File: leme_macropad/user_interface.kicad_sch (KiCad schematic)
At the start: 23 parts, among them J2 OLED display, SW1 RotaryEncoder_Switch, SW10 SW_Push, SW2 SW_Push, SW3 SW_Push, SW4 SW_Push, SW5 SW_Push, SW6 SW_Push, SW7 SW_Push, SW8 SW_Push, SW9 SW_Push

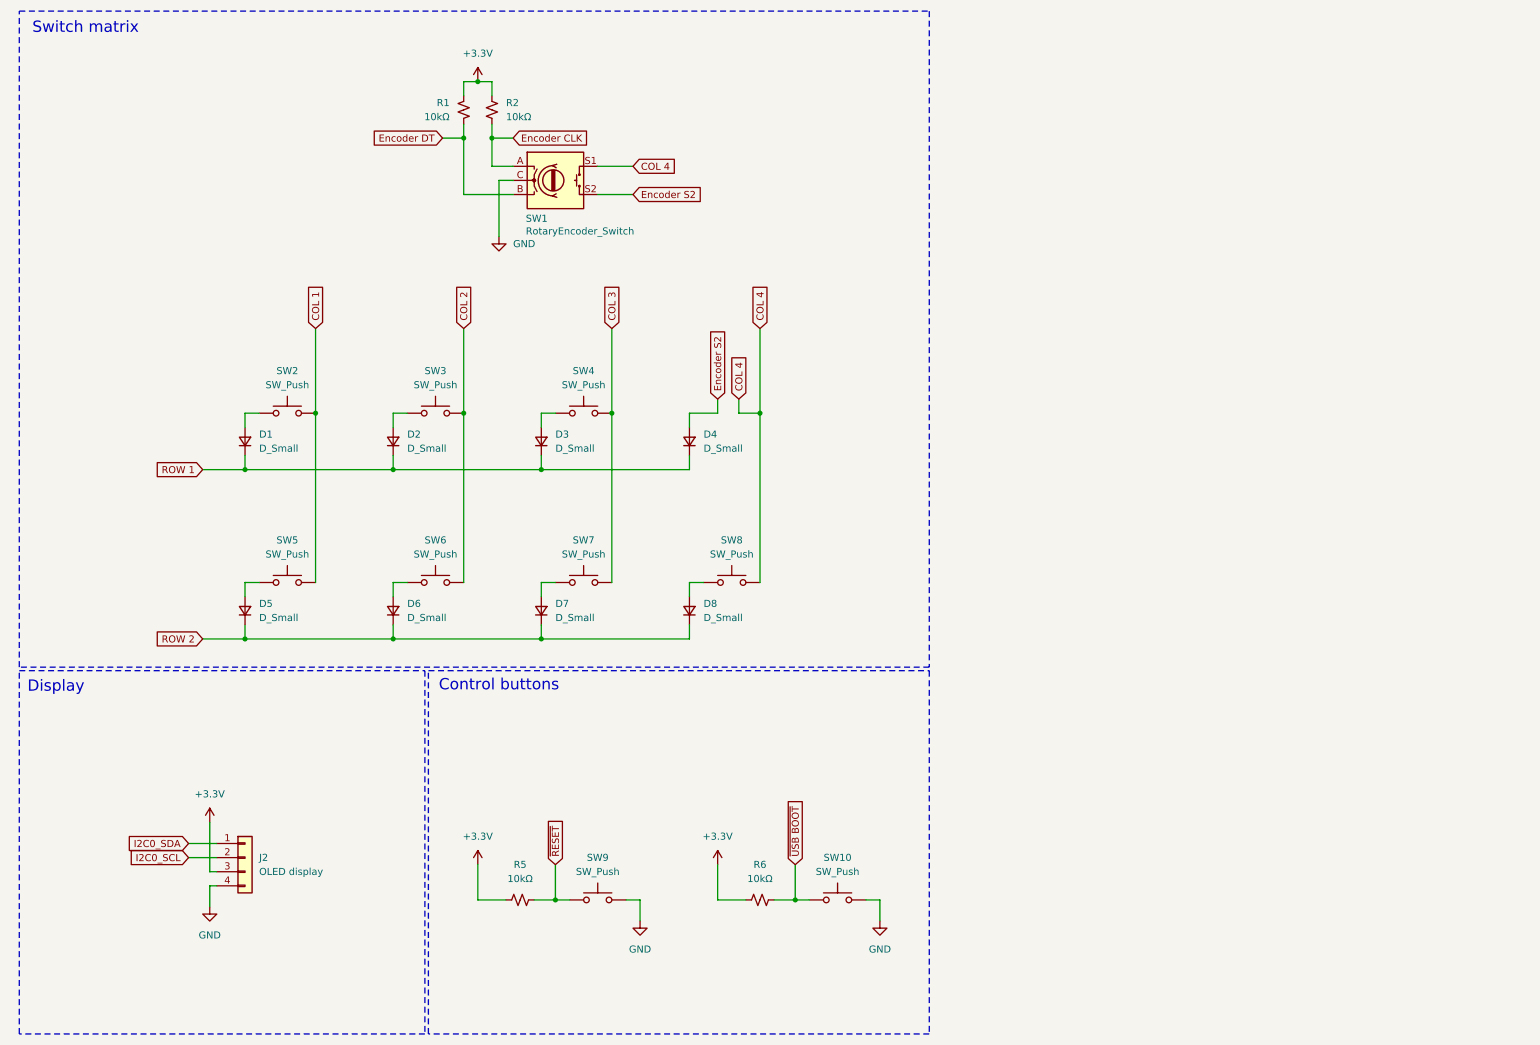
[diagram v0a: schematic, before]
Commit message: Adds RGB LED matrix
There's only one per switch for now.
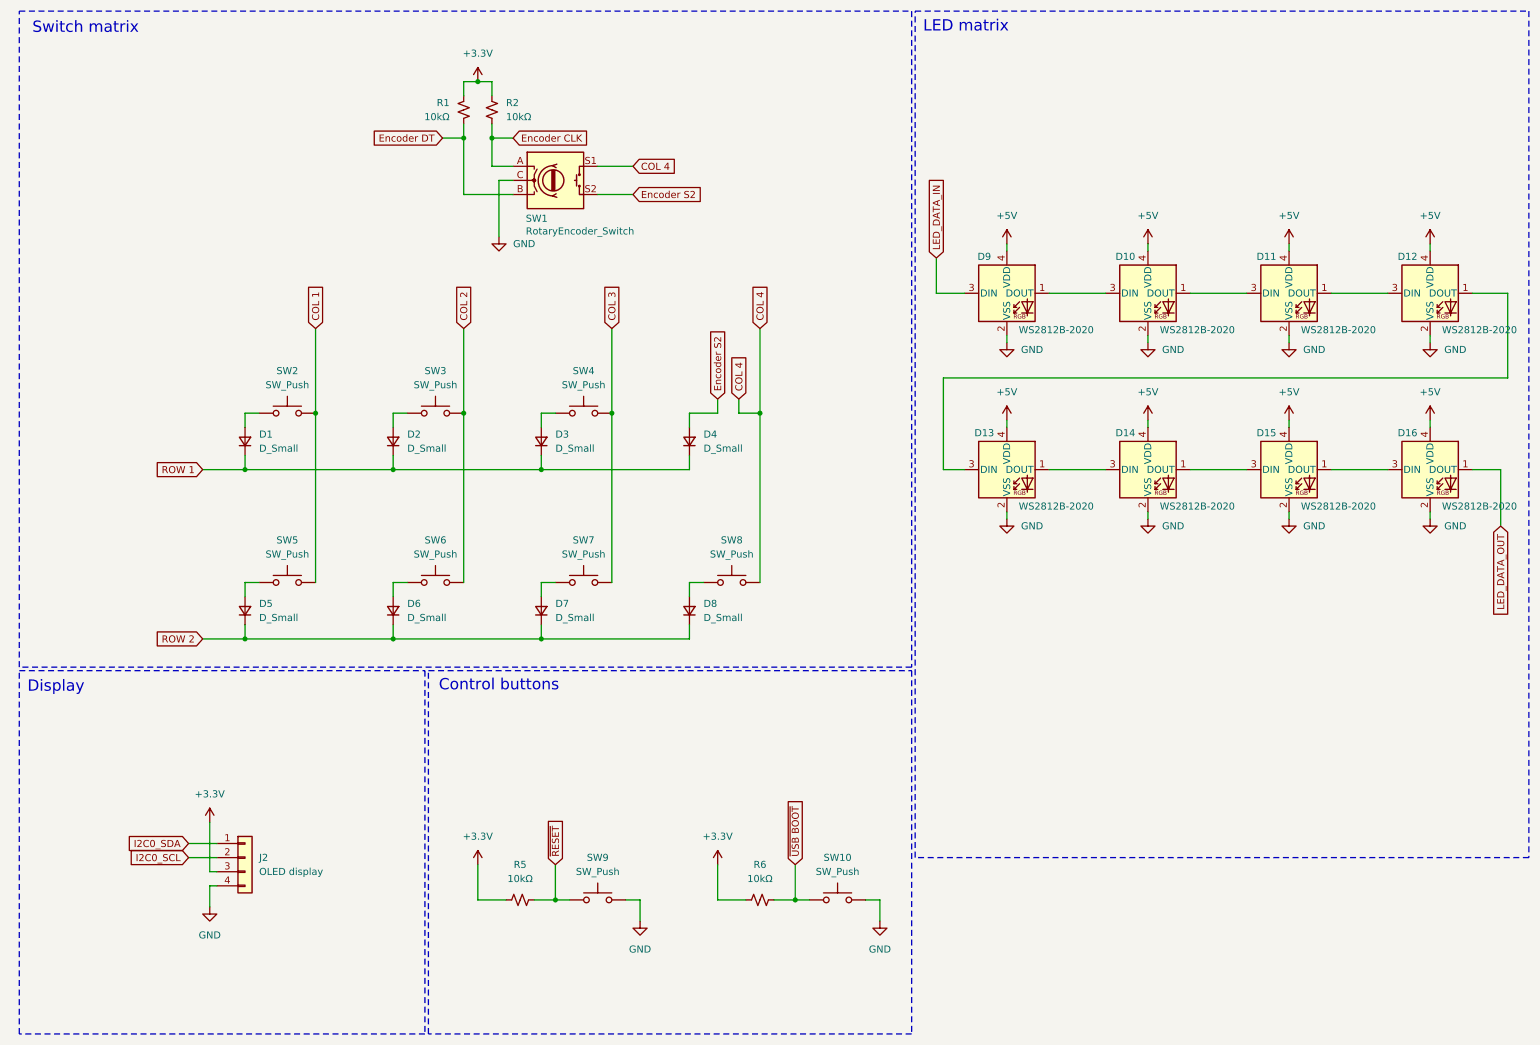
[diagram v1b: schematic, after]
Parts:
- added D10, D11, D12, D13, D14, D15, D16, D9: WS2812B-2020, LED_SMD:LED_WS2812B-2020_PLCC4_2.0x2.0mm, symbol LED:WS2812B-2020
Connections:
- net GND: now also D10.2 (VSS), D11.2 (VSS), D12.2 (VSS), D13.2 (VSS), D14.2 (VSS), D15.2 (VSS), D16.2 (VSS), D9.2 (VSS)
- new net: D14.1 (DOUT), D15.3 (DIN)
- new net: D13.1 (DOUT), D14.3 (DIN)
- new net: D10.3 (DIN), D9.1 (DOUT)
- new net: D12.1 (DOUT), D13.3 (DIN)
- new net: D11.1 (DOUT), D12.3 (DIN)
- new net: D15.1 (DOUT), D16.3 (DIN)
- new net: D10.1 (DOUT), D11.3 (DIN)
- new net +5V: D10.4 (VDD), D11.4 (VDD), D12.4 (VDD), D13.4 (VDD), D14.4 (VDD), D15.4 (VDD), D16.4 (VDD), D9.4 (VDD)
- new net LED_DATA_IN: D9.3 (DIN)
- new net LED_DATA_OUT: D16.1 (DOUT)
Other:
- note added: "LED matrix"

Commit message: Re-annotates schematics
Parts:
- renumbered D5 to D2, D2 to D3, D6 to D4, D3 to D5, D7 to D6, D4 to D7, R2 to R10, R6 to R11, R5 to R8, R1 to R9, SW2 to SW1, SW5 to SW2, SW6 to SW4, SW4 to SW5, SW7 to SW6, SW1 to SW7
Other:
- moved on the sheet: D1, D2, D3, D4, D5, D6, D7, D8, R10, R9, SW1, SW2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

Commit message: Assigns footprints to all components in schematics
Passives are 0603, but if the layout gets too dificult (specially around
the RP2040) we might want to decrease the size.

The mechanical switches are set as hotswap sockets for Kailh v1/v2, but
after routing everything we might want to do a version for MX switches.
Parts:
- D1, D2, D3, D4, D5, D6, D7, D8: footprint (none) -> Diode_SMD:D_SOD-123
- J2: footprint (none) -> Connector_PinHeader_2.54mm:PinHeader_1x04_P2.54mm_Vertical
- R10, R11, R8, R9: footprint (none) -> Resistor_SMD:R_0603_1608Metric_Pad0.98x0.95mm_HandSolder
- SW1, SW2, SW3, SW4, SW5, SW6: footprint (none) -> PCM_Switch_Keyboard_Hotswap_Kailh:SW_Hotswap_Kailh_Choc_V1V2_1.00u
- SW10, SW8, SW9: footprint (none) -> leme_macropad:CK_PTS636_SK43_SMTR_LFS
- SW7: footprint (none) -> Rotary_Encoder:RotaryEncoder_Alps_EC11E-Switch_Vertical_H20mm
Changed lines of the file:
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@@
 			)
 		)
-		(property "Footprint" ""
+		(property "Footprint" "leme_macropad:CK_PTS636_SK43_SMTR_LFS"
 			(at 160.02 167.64 0)
 			(effects
@@
 			)
 		)
-		(property "Footprint" ""
+		(property "Footprint" "Diode_SMD:D_SOD-123"
 			(at 87.63 90.17 90)
 			(effects
@@
 			)
 		)
-		(property "Footprint" ""
+		(property "Footprint" "Diode_SMD:D_SOD-123"
 			(at 60.96 90.17 90)
 			(effects
@@
 			)
 		)
-		(property "Footprint" ""
+		(property "Footprint" "Diode_SMD:D_SOD-123"
 			(at 34.29 120.65 90)
 			(effects
@@
 			)
 		)
-		(property "Footprint" ""
+		(property "Footprint" "Resistor_SMD:R_0603_1608Metric_Pad0.98x0.95mm_HandSolder"
 			(at 113.03 30.48 0)
 			(effects
@@
 			)
 		)
-		(property "Footprint" ""
+		(property "Footprint" "Resistor_SMD:R_0603_1608Metric_Pad0.98x0.95mm_HandSolder"
 			(at 146.05 172.72 0)
 			(effects
@@
 			)
 		)
-		(property "Footprint" ""
+		(property "Footprint" "Rotary_Encoder:RotaryEncoder_Alps_EC11E-Switch_Vertical_H20mm"
 			(at 120.65 39.116 0)
 			(effects
@@
 			)
 		)
-		(property "Footprint" ""
+		(property "Footprint" "Diode_SMD:D_SOD-123"
 			(at 114.3 90.17 90)
 			(effects
@@
 			)
 		)
-		(property "Footprint" ""
+		(property "Footprint" "PCM_Switch_Keyboard_Hotswap_Kailh:SW_Hotswap_Kailh_Choc_V1V2_1.00u"
 			(at 41.91 110.49 0)
 			(effects
@@
 			)
 		)
-		(property "Footprint" ""
+		(property "Footprint" "Diode_SMD:D_SOD-123"
 			(at 114.3 120.65 90)
 			(effects
@@
 			)
 		)
-		(property "Footprint" ""
+		(property "Footprint" "leme_macropad:CK_PTS636_SK43_SMTR_LFS"
 			(at 116.84 167.64 0)
 			(effects
@@
 			)
 		)
-		(property "Footprint" ""
+		(property "Footprint" "PCM_Switch_Keyboard_Hotswap_Kailh:SW_Hotswap_Kailh_Choc_V1V2_1.00u"
 			(at 68.58 110.49 0)
 			(effects
@@
 			)
 		)
-		(property "Footprint" ""
+		(property "Footprint" "PCM_Switch_Keyboard_Hotswap_Kailh:SW_Hotswap_Kailh_Choc_V1V2_1.00u"
 			(at 95.25 80.01 0)
 			(effects
@@
 			)
 		)
-		(property "Footprint" ""
+		(property "Footprint" "Connector_PinHeader_2.54mm:PinHeader_1x04_P2.54mm_Vertical"
 			(at 53.34 165.1 0)
 			(effects
@@
 			)
 		)
-		(property "Footprint" ""
+		(property "Footprint" "PCM_Switch_Keyboard_Hotswap_Kailh:SW_Hotswap_Kailh_Choc_V1V2_1.00u"
 			(at 41.91 80.01 0)
 			(effects
@@
 			)
 		)
-		(property "Footprint" ""
+		(property "Footprint" "Diode_SMD:D_SOD-123"
 			(at 34.29 90.17 90)
 			(effects
@@
 			)
 		)
-		(property "Footprint" ""
+		(property "Footprint" "Diode_SMD:D_SOD-123"
 			(at 87.63 120.65 90)
 			(effects
@@
 			)
 		)
-		(property "Footprint" ""
+		(property "Footprint" "Resistor_SMD:R_0603_1608Metric_Pad0.98x0.95mm_HandSolder"
 			(at 107.95 30.48 0)
 			(effects
@@
 			)
 		)
-		(property "Footprint" ""
+		(property "Footprint" "PCM_Switch_Keyboard_Hotswap_Kailh:SW_Hotswap_Kailh_Choc_V1V2_1.00u"
 			(at 95.25 110.49 0)
 			(effects
@@
 			)
 		)
-		(property "Footprint" ""
+		(property "Footprint" "Diode_SMD:D_SOD-123"
 			(at 60.96 120.65 90)
 			(effects
@@
 			)
 		)
-		(property "Footprint" ""
+		(property "Footprint" "PCM_Switch_Keyboard_Hotswap_Kailh:SW_Hotswap_Kailh_Choc_V1V2_1.00u"
 			(at 68.58 80.01 0)
 			(effects
@@
 			)
 		)
-		(property "Footprint" ""
+		(property "Footprint" "Resistor_SMD:R_0603_1608Metric_Pad0.98x0.95mm_HandSolder"
 			(at 102.87 172.72 0)
 			(effects
@@
 			)
 		)
-		(property "Footprint" ""
+		(property "Footprint" "leme_macropad:CK_PTS636_SK43_SMTR_LFS"
 			(at 121.92 110.49 0)
 			(effects

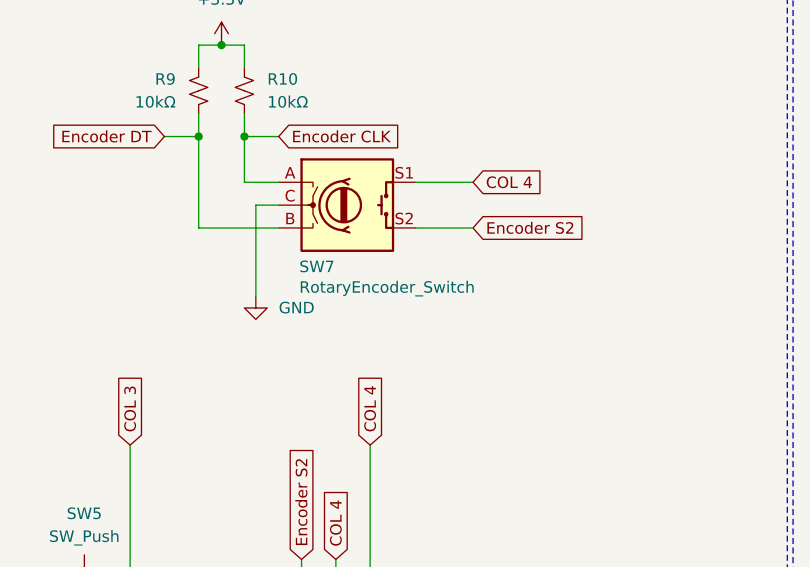
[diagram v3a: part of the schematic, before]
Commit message: Uses rotary encoder symbol with mounting pin
The rotary switch we'll use has mounting pins that can be soldered.
Since they're connected to the chassis, they're now connected to ground
in the schematics.

This change fixes a warning when importing the schematics to the PCB
editor.
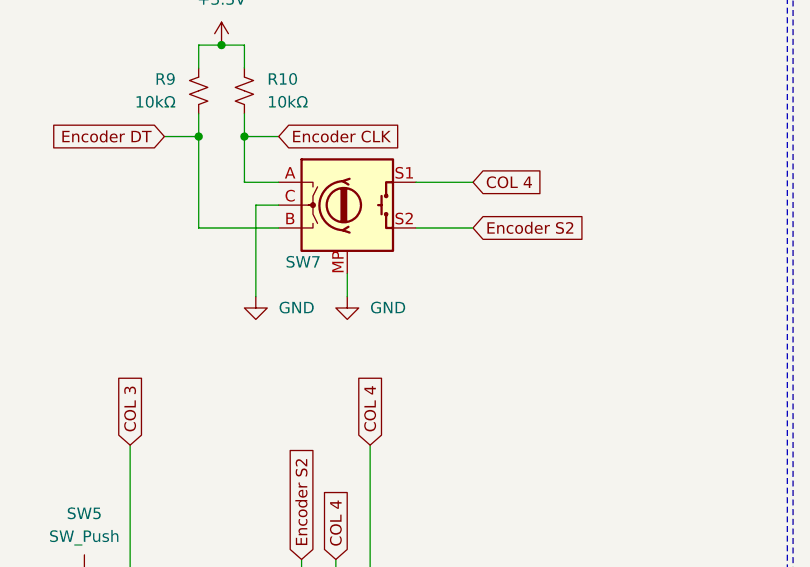
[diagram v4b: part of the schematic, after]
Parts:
- SW7: symbol Device:RotaryEncoder_Switch -> Device:RotaryEncoder_Switch_MP
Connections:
- net GND: now also SW7.MP
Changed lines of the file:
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@@
+	(wire
+		(pts
+			(xy 124.46 50.8) (xy 124.46 53.34)
+		)
+		(stroke
+			(width 0)
+			(type default)
+		)
+	)
 	(wire
 		(pts
@@
 	)
 	(symbol
+		(lib_id "power:GND")
+		(at 124.46 53.34 0)
+		(unit 1)
+		(exclude_from_sim no)
+		(in_bom yes)
+		(on_board yes)
+		(dnp no)
+		(fields_autoplaced yes)
+		(property "Reference" "#PWR063"
+			(at 124.46 59.69 0)
+			(effects
+				(font
+					(size 1.27 1.27)
+				)
+				(hide yes)
+			)
+		)
+		(property "Value" "GND"
+			(at 127 54.6099 0)
+			(effects
+				(font
+					(size 1.27 1.27)
+				)
+				(justify left)
+			)
+		)
+		(property "Footprint" ""
+			(at 124.46 53.34 0)
+			(effects
+				(font
+					(size 1.27 1.27)
+				)
+				(hide yes)
+			)
+		)
+		(property "Datasheet" ""
+			(at 124.46 53.34 0)
+			(effects
+				(font
+					(size 1.27 1.27)
+				)
+				(hide yes)
+			)
+		)
+		(property "Description" "Power symbol creates a global label with name \"GND\" , ground"
+			(at 124.46 53.34 0)
+			(effects
+				(font
+					(size 1.27 1.27)
+				)
+				(hide yes)
+			)
+		)
+		(pin "1"
+		)
+		(instances
+			(project "leme_macropad"
+				(path "/a37365a2-c635-4451-9354-78f9e753d687/b6fad1bd-9b8b-42cb-b41f-ac701051e19c"
+					(reference "#PWR063")
+					(unit 1)
+				)
+			)
+		)
+	)
+	(symbol
 		(lib_id "Device:R_Small_US")
 		(at 146.05 172.72 90)
@@
 	)
 	(symbol
-		(lib_id "Device:RotaryEncoder_Switch")
+		(lib_id "Device:RotaryEncoder_Switch_MP")
 		(at 124.46 43.18 0)
 		(unit 1)
@@
 		(dnp no)
 		(property "Reference" "SW7"
-			(at 119.126 50.038 0)
+			(at 117.602 49.53 0)
 			(effects
 				(font
@@
 				)
 				(justify left)
+				(hide yes)
 			)
 		)
@@
 		)
 		(property "Datasheet" "~"
-			(at 124.46 36.576 0)
-			(effects
-				(font
-					(size 1.27 1.27)
-				)
-				(hide yes)
-			)
-		)
-		(property "Description" "Rotary encoder, dual channel, incremental quadrate outputs, with switch"
-			(at 124.46 43.18 0)
+			(at 124.46 55.88 0)
+			(effects
+				(font
+					(size 1.27 1.27)
+				)
+				(hide yes)
+			)
+		)
+		(property "Description" "Rotary encoder, dual channel, incremental quadrate outputs, with switch and MP Pin"
+			(at 124.46 58.42 0)
 			(effects
 				(font
@@
 		(pin "B"
 		)
-		(instances
+		(pin "MP"
+		)
+		(instances

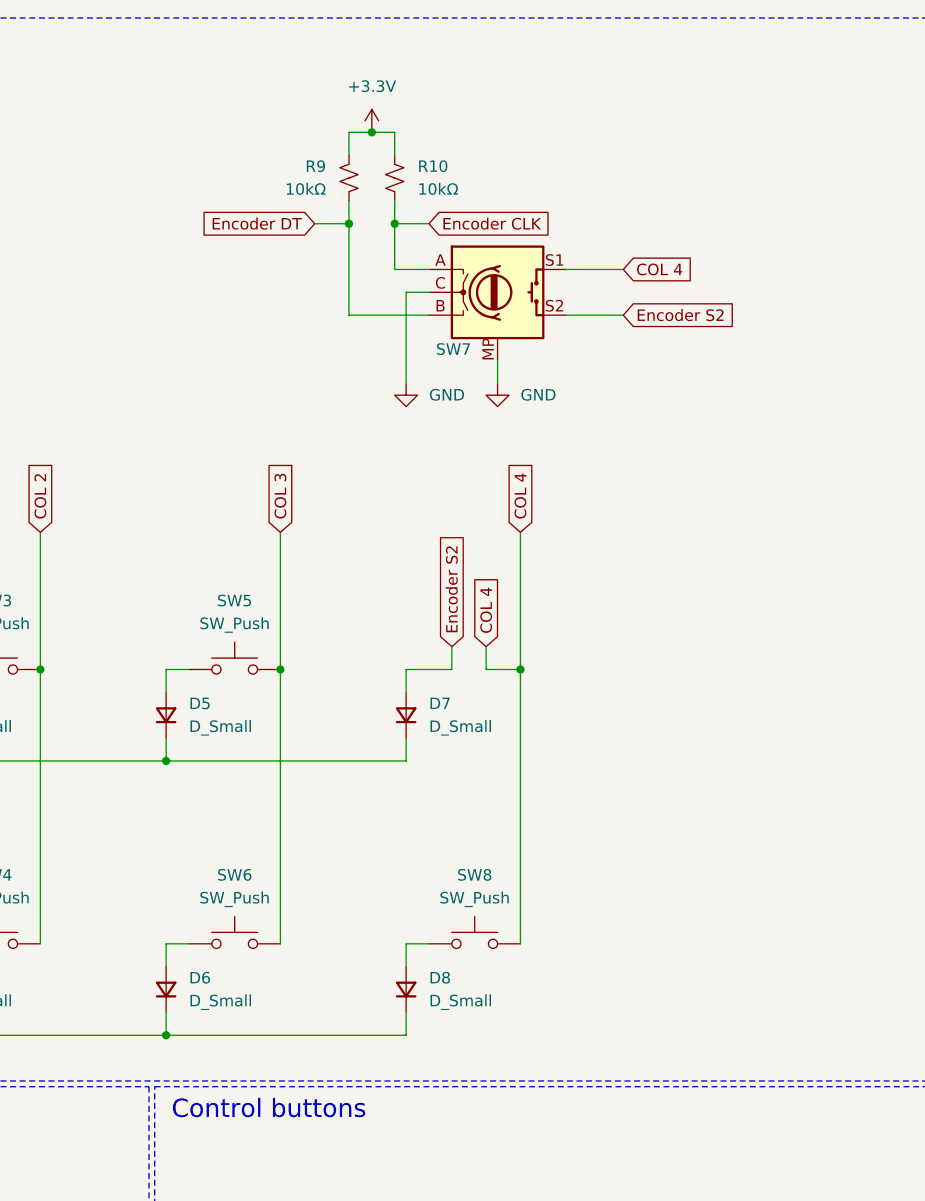
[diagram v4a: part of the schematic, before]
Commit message: Removes SW8
This button was there just to complete the matrix but we have no use for
it. It would only make things harder to organize.
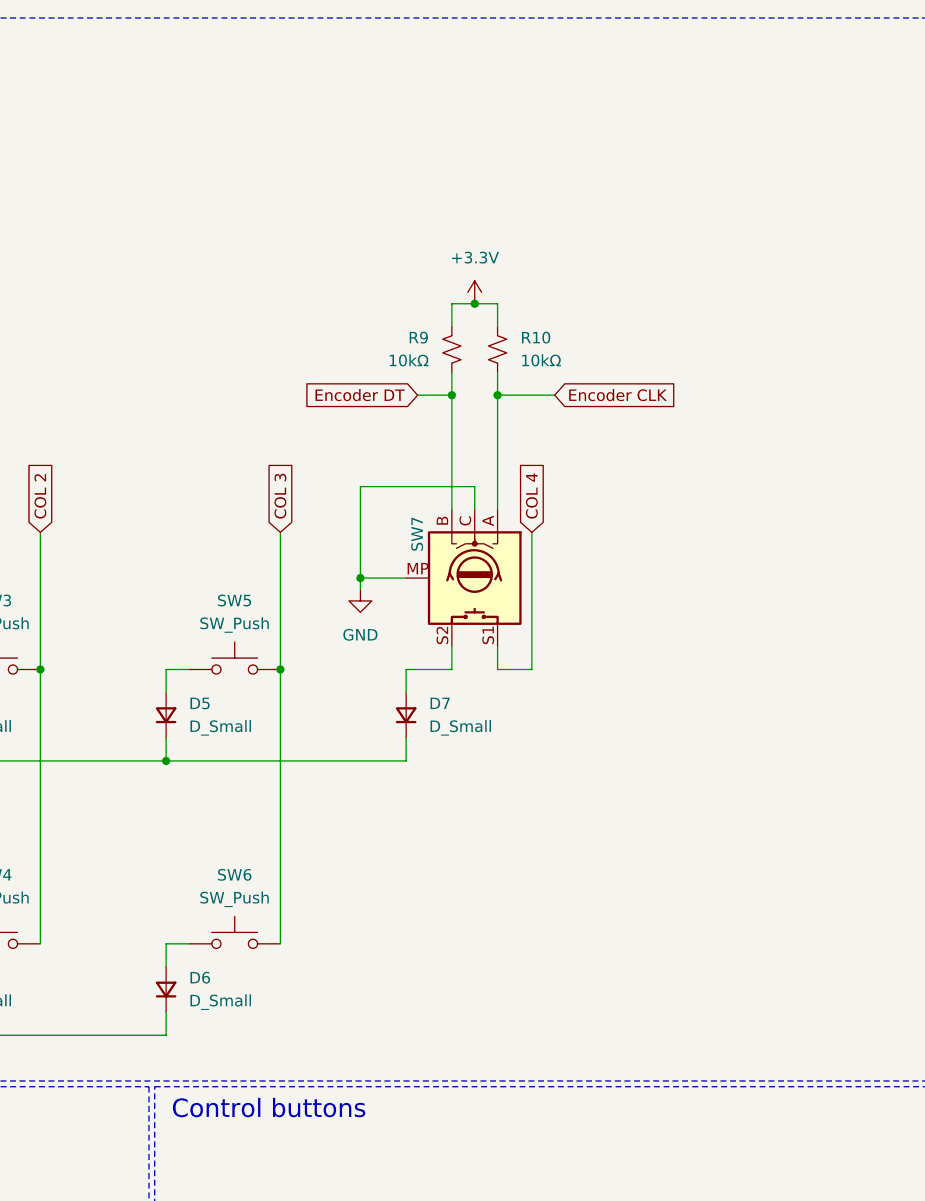
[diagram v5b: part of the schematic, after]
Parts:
- removed D8: D_Small, Diode_SMD:D_SOD-123, symbol Device:D_Small
- removed SW8: SW_Push, leme_macropad:CK_PTS636_SK43_SMTR_LFS, symbol Switch:SW_Push
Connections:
- net Encoder S2: no longer names the net of D7.2 (A), SW7.S2
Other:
- moved on the sheet: R10, R9, SW7

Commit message: Changes resistors and capacitors to 0402
This should make it much easier to route things and to comply with the
signal integrity needs of some parts of the circuit.
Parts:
- R10, R11, R8, R9: footprint Resistor_SMD:R_0603_1608Metric_Pad0.98x0.95mm_HandSolder -> Resistor_SMD:R_0402_1005Metric_Pad0.72x0.64mm_HandSolder
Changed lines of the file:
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@@
 			)
 		)
-		(property "Footprint" "Resistor_SMD:R_0603_1608Metric_Pad0.98x0.95mm_HandSolder"
+		(property "Footprint" "Resistor_SMD:R_0402_1005Metric_Pad0.72x0.64mm_HandSolder"
 			(at 124.46 49.53 0)
 			(effects
@@
 			)
 		)
-		(property "Footprint" "Resistor_SMD:R_0603_1608Metric_Pad0.98x0.95mm_HandSolder"
+		(property "Footprint" "Resistor_SMD:R_0402_1005Metric_Pad0.72x0.64mm_HandSolder"
 			(at 146.05 172.72 0)
 			(effects
@@
 			)
 		)
-		(property "Footprint" "Resistor_SMD:R_0603_1608Metric_Pad0.98x0.95mm_HandSolder"
+		(property "Footprint" "Resistor_SMD:R_0402_1005Metric_Pad0.72x0.64mm_HandSolder"
 			(at 119.38 49.53 0)
 			(effects
@@
 			)
 		)
-		(property "Footprint" "Resistor_SMD:R_0603_1608Metric_Pad0.98x0.95mm_HandSolder"
+		(property "Footprint" "Resistor_SMD:R_0402_1005Metric_Pad0.72x0.64mm_HandSolder"
 			(at 102.87 172.72 0)
 			(effects
